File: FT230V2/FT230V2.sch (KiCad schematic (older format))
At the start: 19 parts, among them J1 Conn_01x06, P1 USB_C_Plug_USB2.0, U1 FT230XQ

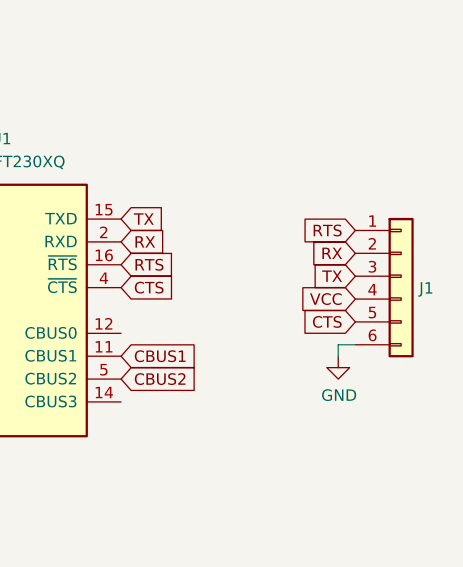
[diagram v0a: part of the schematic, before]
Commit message: SiRUSB Updates
USB-C 3D Renders Added and Pictures Updated
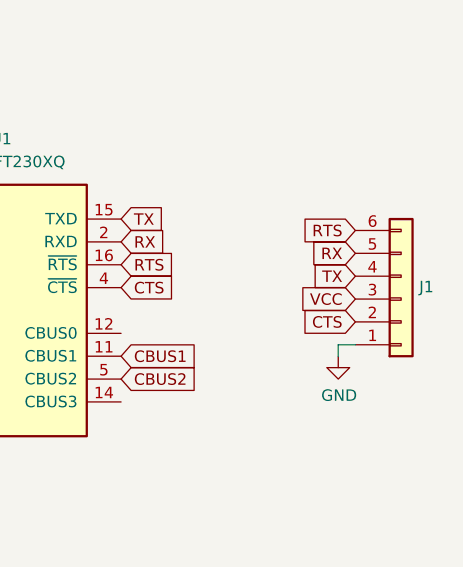
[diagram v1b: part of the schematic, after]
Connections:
- net CTS: now also J1.2 (Pin_2); no longer J1.5 (Pin_5)
- net GND: now also J1.1 (Pin_1); no longer J1.6 (Pin_6)
- net RTS: now also J1.6 (Pin_6); no longer J1.1 (Pin_1)
- net RX: now also J1.5 (Pin_5); no longer J1.2 (Pin_2)
- net TX: now also J1.4 (Pin_4); no longer J1.3 (Pin_3)
- net VCC: now also J1.3 (Pin_3); no longer J1.4 (Pin_4)
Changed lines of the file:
@@
 L Connector_Generic:Conn_01x06 J1
 U 1 1 5E4934CD
-P 7500 2025
-F 0 "J1" H 7579 1972 50  0000 L CNN
-F 1 "Conn_01x06" H 7579 1927 50  0001 L CNN
-F 2 "Connector_PinHeader_2.54mm:PinHeader_1x06_P2.54mm_Vertical" H 7500 2025 50  0001 C CNN
-F 3 "~" H 7500 2025 50  0001 C CNN
-	1    7500 2025
-	1    0    0    -1
+P 7500 2125
+F 0 "J1" H 7579 2072 50  0000 L CNN
+F 1 "Conn_01x06" H 7579 2027 50  0001 L CNN
+F 2 "Connector_PinHeader_2.54mm:PinHeader_1x06_P2.54mm_Vertical" H 7500 2125 50  0001 C CNN
+F 3 "~" H 7500 2125 50  0001 C CNN
+	1    7500 2125
+	1    0    0    1
 $EndComp
 Text GLabel 7300 2025 0    50   Input ~ 0

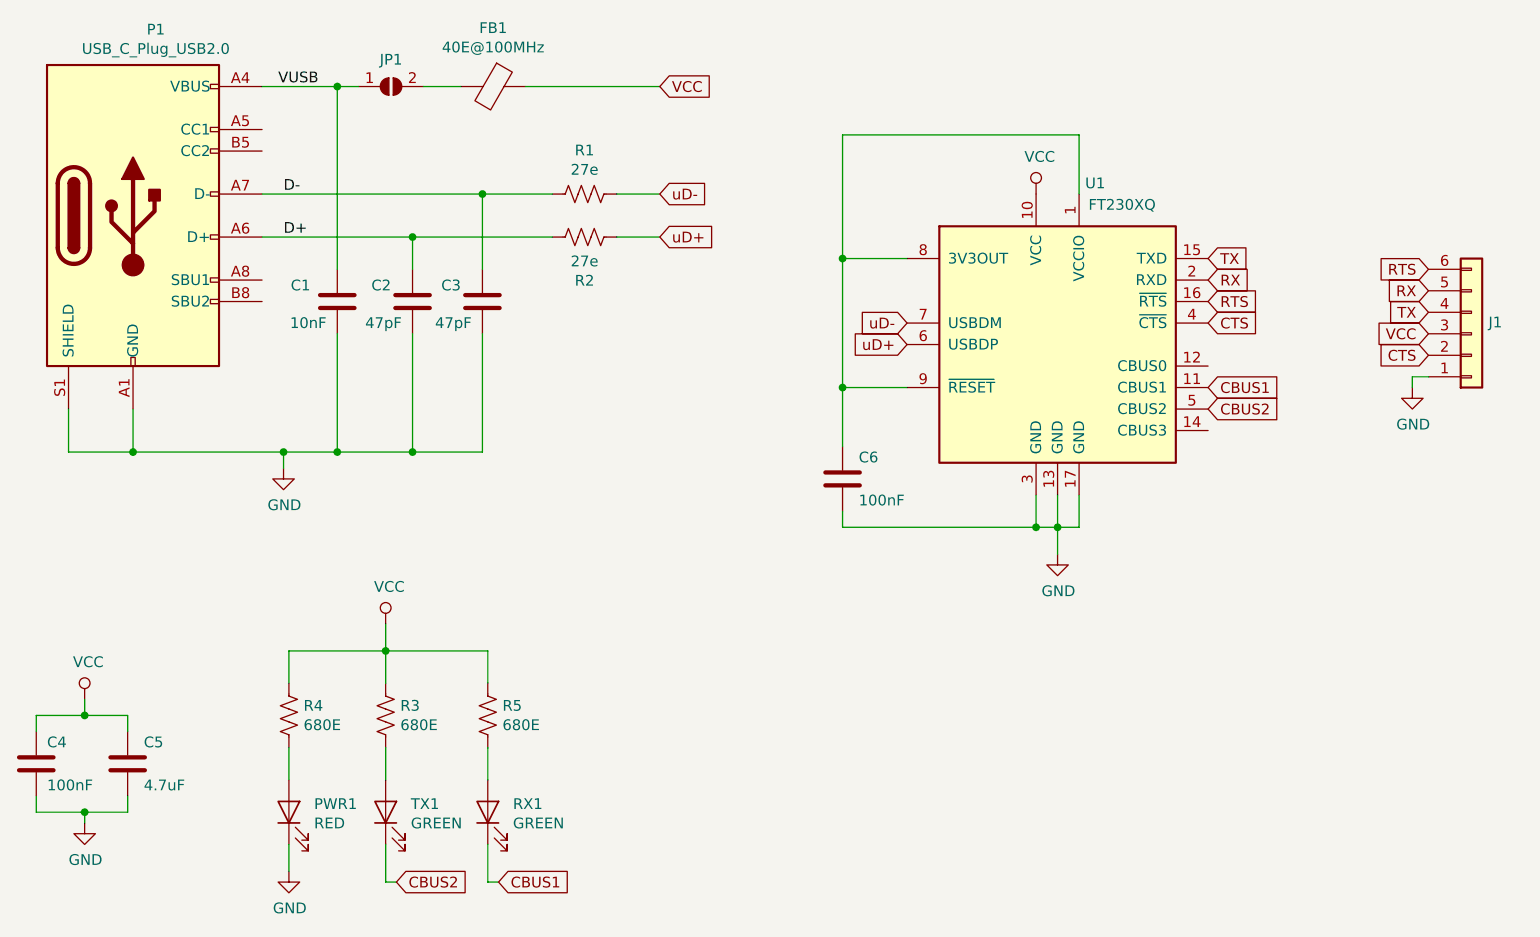
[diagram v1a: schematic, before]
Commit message: SirUSB Board Revisions
Removed MicroUSB Versions of FT230 and FT231, SolderPaste Layer Adjusted to -0.05mm, Silkscreens optimised, OSHW logo added.
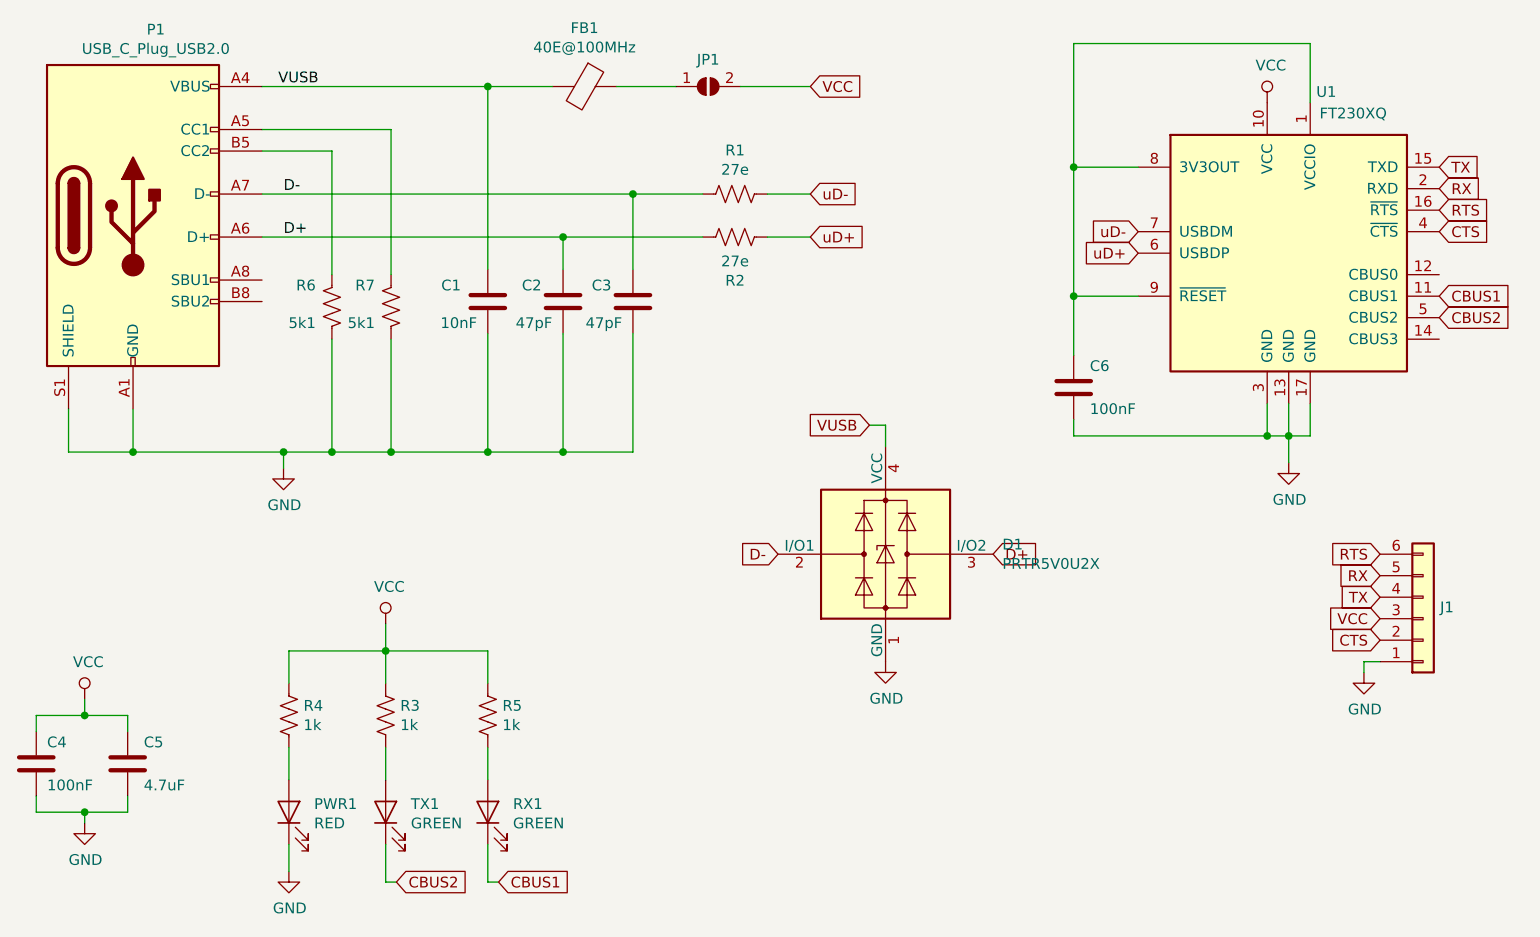
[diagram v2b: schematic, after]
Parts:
- added D1: PRTR5V0U2X, SirBoardLibrary:SOT-143, symbol Power_Protection:PRTR5V0U2X
- added R6, R7: 5k1, Resistor_SMD:R_0603_1608Metric, symbol Device:R_US
- R3, R4, R5: value 680E -> 1k; Part C269441 -> C25585
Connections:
- net D+: now also D1.3 (I/O2)
- net D-: now also D1.2 (I/O1)
- net GND: now also D1.1 (GND), R6.2, R7.2
- net VCC: now also JP1.2 (B); no longer FB1.1
- net VUSB: now also FB1.2, D1.4 (VCC); no longer JP1.1 (A)
- net at P1.A5 (CC1): now also R7.1
- net at P1.B5 (CC2): now also R6.1
- new net: FB1.1, JP1.1 (A)
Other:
- moved on the sheet: C1, C2, C3, C6, FB1, J1, JP1, R1, R2, U1
